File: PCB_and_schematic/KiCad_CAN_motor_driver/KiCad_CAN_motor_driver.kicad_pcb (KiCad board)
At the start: 2 copper layers, 90.4 x 45.2 mm, 67 parts, among them J1 SWDIO, J2 UART, J3 POWER IN 24V, J4 MOTOR OUT, J5 CAN, J6 PWM IN, Q1 BTN8982TA, Q2 BTN8982TA, U1 SN65HVD232, U2 LMR50410, U3 STM32F103C8Tx

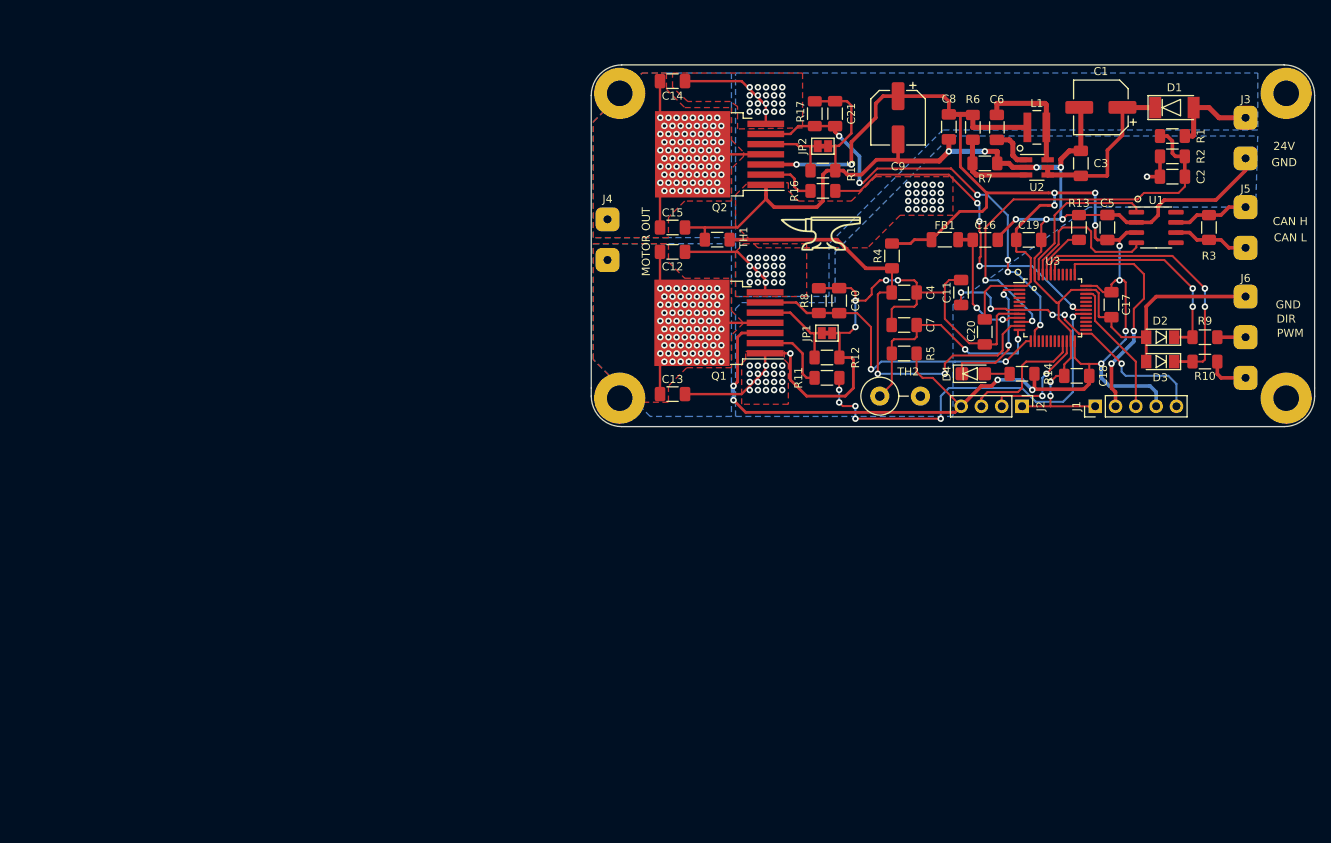
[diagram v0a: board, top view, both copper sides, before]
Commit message: Power traces optimization
+power traces optimized for lower resistance
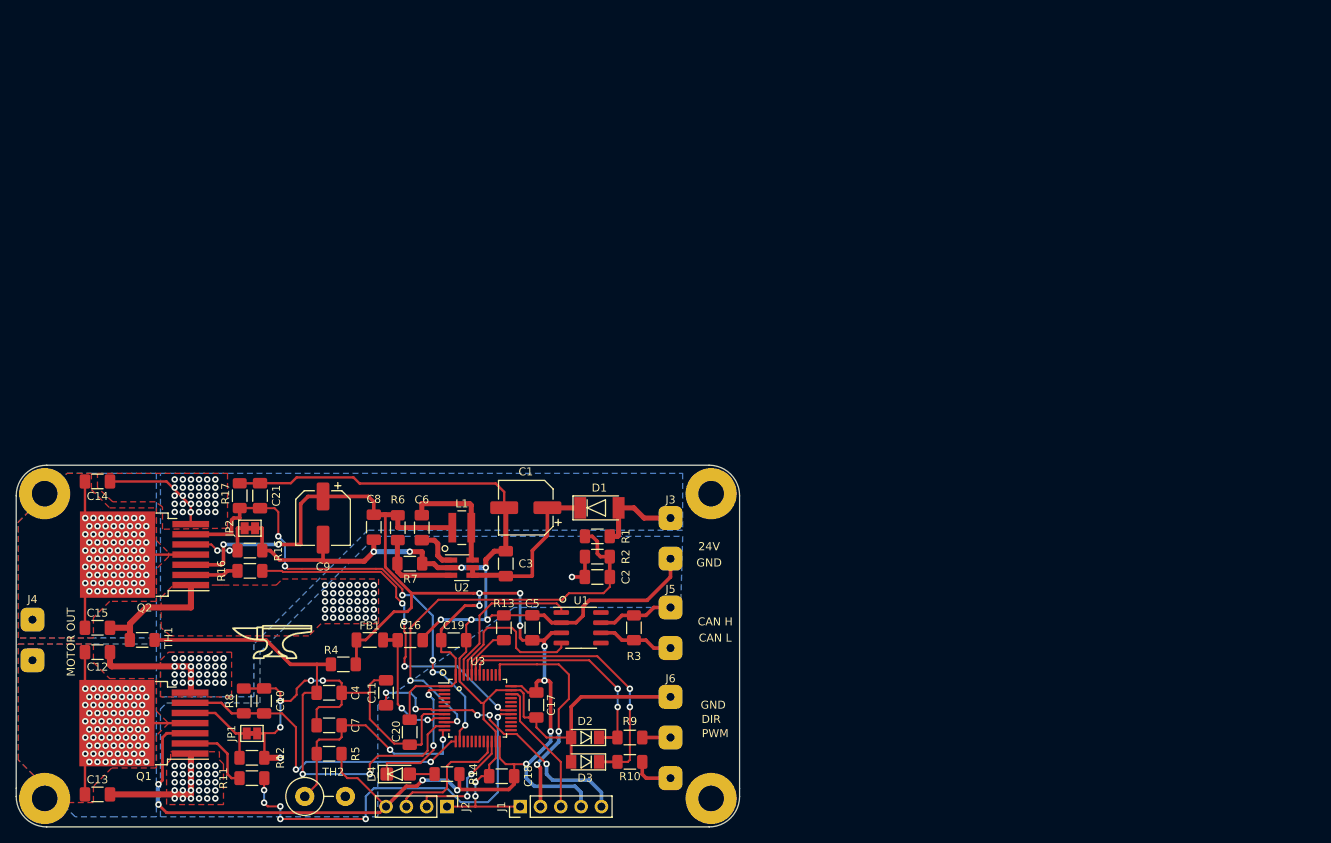
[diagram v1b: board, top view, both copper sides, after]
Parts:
- moved J3 87.6 mm to (187.7, 86.1)
- moved J5 87.6 mm to (187.7, 97.3)
- moved J6 87.6 mm to (187.7, 108.5)
- moved R10 87.6 mm to (182.6, 114.0)
- moved REF** 87.6 mm to (145.5, 81.5)
- moved TH2 87.6 mm to (142.0, 118.4)
- moved C1 87.6 mm to (169.6, 82.3)
- moved C10 87.6 mm to (136.9, 106.4)
- moved C11 87.6 mm to (152.1, 105.4)
- moved C12 87.6 mm to (116.1, 100.3)
- moved C13 87.6 mm to (116.1, 118.1)
- moved C14 87.6 mm to (116.1, 79.0)
- moved C15 87.6 mm to (116.1, 97.3)
- moved C16 87.6 mm to (155.2, 98.8)
- moved C17 87.6 mm to (170.9, 106.9)
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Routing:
- net GND: track 301.4 -> 296.8 mm, vias 55 -> 80
- net /I_SENSE_2: track 57.4 -> 61.2 mm
- net /NTC_INTERNAL: track 58.7 -> 60.8 mm
- net +24V: track 38.3 -> 40.4 mm, vias 40 -> 58
- net Net-(Q2-Pad2): track 7.03 -> 6.06 mm
- net +3V3: track 232.7 -> 233.5 mm
- net Net-(JP2-Pad1): track 9.65 -> 9.84 mm, vias 0 -> 2
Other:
- net class Default: clearance 0.2032 -> 0.127
- rule trace_clearance: 0.2032 -> 0.127
- board text added: "Rev 1.0"

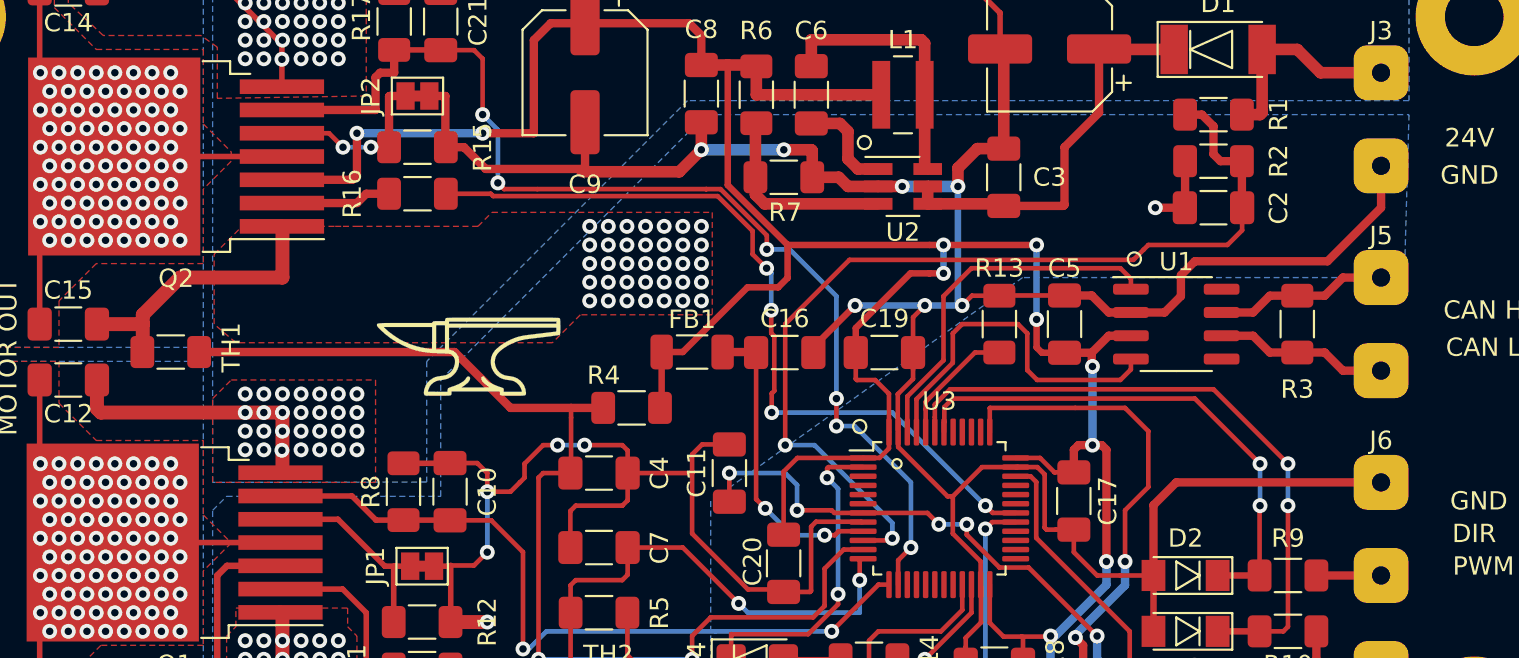
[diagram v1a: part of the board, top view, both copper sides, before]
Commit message: PDF schematic
+ schematic in PDF format for quick preview
+ changed resistors on PWM inputs from 1K to 6.8K to decrease Zener diodes current
+ little tweaks in PCB traces
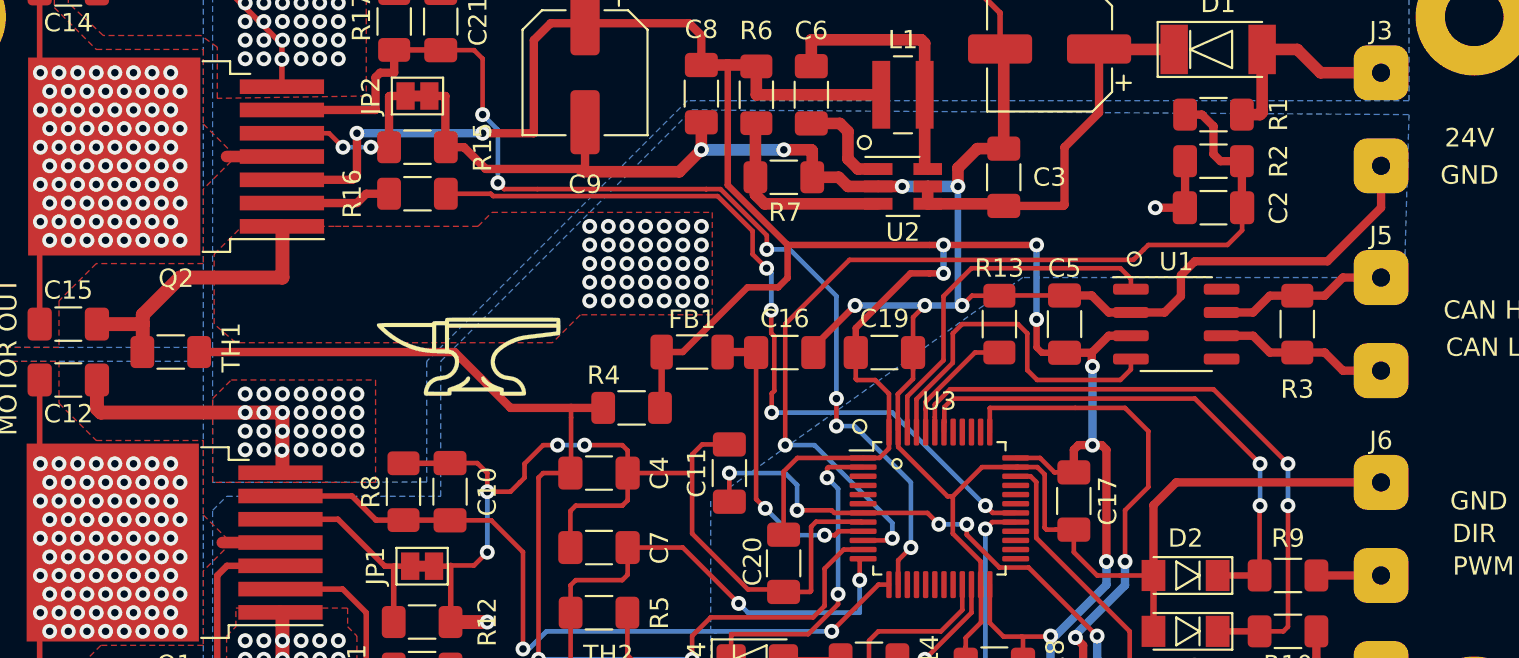
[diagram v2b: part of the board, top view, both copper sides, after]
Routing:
- net /MOT_B: track 30.8 -> 24.7 mm
- net /MOT_A: track 30.2 -> 24.3 mm
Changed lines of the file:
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@@
   (via (at 115.57 108.966) (size 0.8128) (drill 0.4064) (layers F.Cu B.Cu) (net 11))
   (via (at 119.634 110.998) (size 0.8128) (drill 0.4064) (layers F.Cu B.Cu) (net 11))
-  (segment (start 127.653 109.201) (end 118.503 109.201) (width 0.3048) (layer F.Cu) (net 11))
   (segment (start 114.5155 113.1885) (end 118.503 109.201) (width 0.3048) (layer F.Cu) (net 11))
   (segment (start 114.5155 118.11) (end 114.5155 113.1885) (width 0.3048) (layer F.Cu) (net 11))
   (segment (start 114.5155 105.2135) (end 118.503 109.201) (width 0.3048) (layer F.Cu) (net 11))
   (segment (start 114.5155 100.33) (end 114.5155 105.2135) (width 0.3048) (layer F.Cu) (net 11))
+  (segment (start 127.653 109.201) (end 124.479 109.201) (width 0.635) (layer F.Cu) (net 11))
   (via (at 130.81 80.772) (size 0.8128) (drill 0.4064) (layers F.Cu B.Cu) (net 12))
   (via (at 130.81 81.788) (size 0.8128) (drill 0.4064) (layers F.Cu B.Cu) (net 12))
@@
   (segment (start 114.5155 84.0705) (end 118.583 88.138) (width 0.3048) (layer F.Cu) (net 13))
   (segment (start 114.5155 78.994) (end 114.5155 84.0705) (width 0.3048) (layer F.Cu) (net 13))
-  (segment (start 127.733 88.138) (end 118.583 88.138) (width 0.3048) (layer F.Cu) (net 13))
   (segment (start 114.5155 92.2055) (end 118.583 88.138) (width 0.3048) (layer F.Cu) (net 13))
   (segment (start 114.5155 97.282) (end 114.5155 92.2055) (width 0.3048) (layer F.Cu) (net 13))
+  (segment (start 127.733 88.138) (end 124.714 88.138) (width 0.635) (layer F.Cu) (net 13))
   (segment (start 153.4435 98.9965) (end 153.606 98.834) (width 0.635) (layer F.Cu) (net 14))
   (via (at 154.106 107.334) (size 0.8128) (drill 0.4064) (layers F.Cu B.Cu) (net 14))
@@
       (pts
         (xy 188.976 94.742) (xy 168.148 94.742) (xy 151.13 106.934) (xy 151.13 120.904) (xy 123.952 120.904)
-        (xy 123.952 107.442) (xy 124.714 106.68) (xy 136.398 106.68) (xy 136.398 100.33) (xy 150.876 85.852)
+        (xy 123.952 107.442) (xy 124.714 106.68) (xy 136.398 106.68) (xy 136.398 99.314) (xy 150.114 85.598)
         (xy 189.23 85.852)
       )

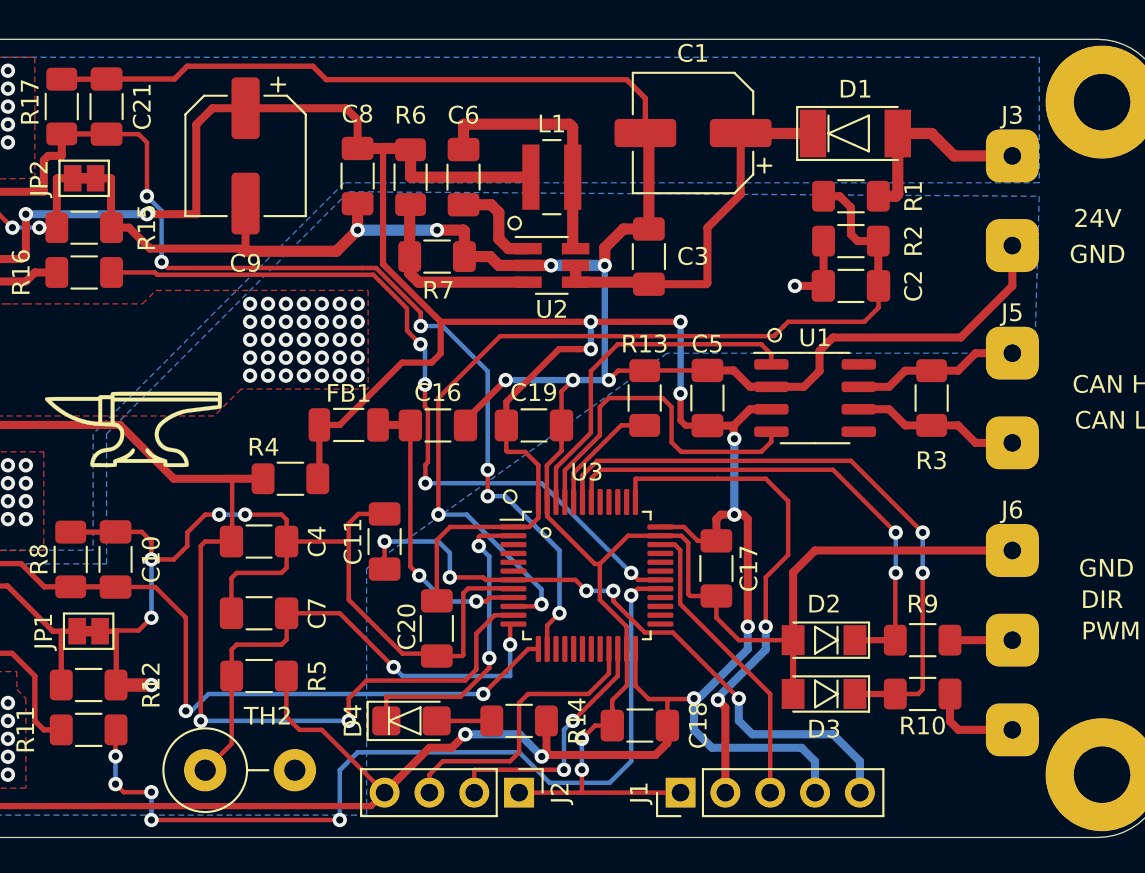
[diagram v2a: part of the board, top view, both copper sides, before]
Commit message: Added vias on power traces near input, added testpoints
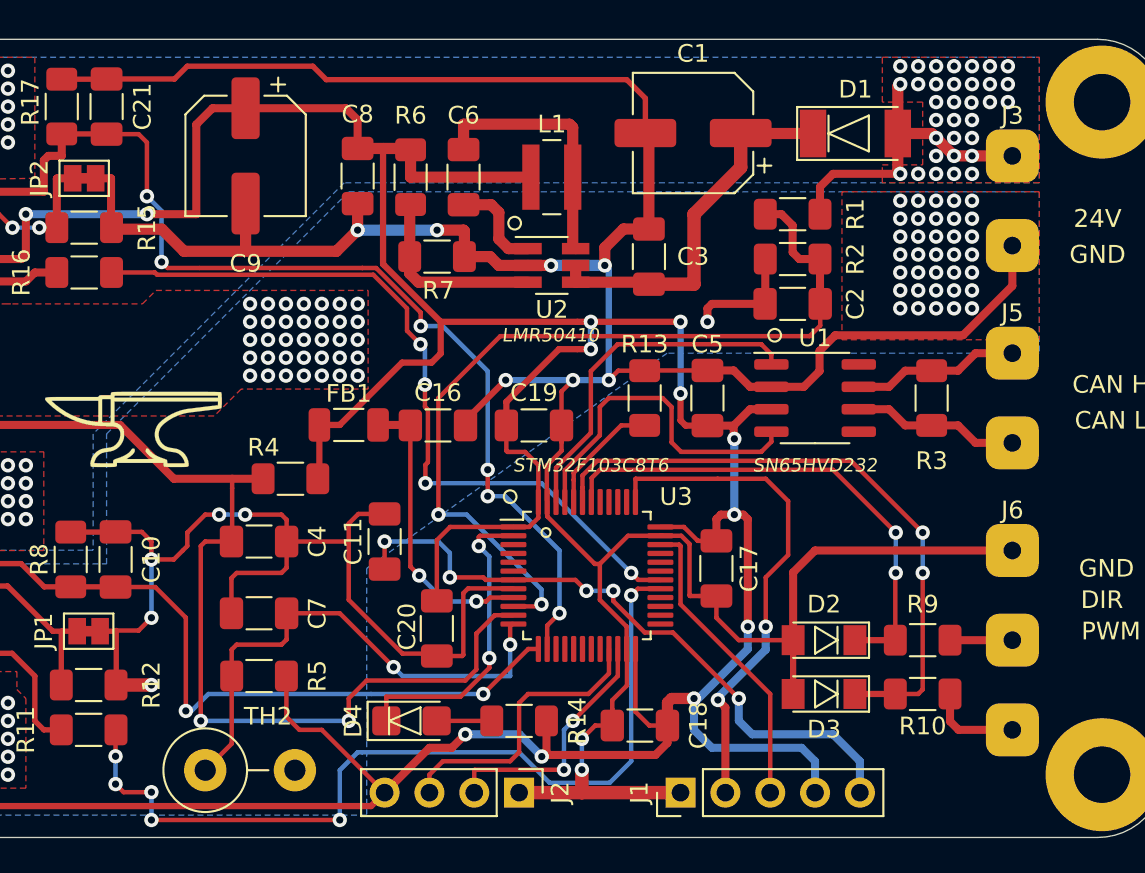
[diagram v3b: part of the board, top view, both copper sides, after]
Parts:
- moved R2 3.45 mm to (175.3, 89.4)
- moved C2 3.45 mm to (175.3, 91.9)
- moved R1 3.45 mm to (175.3, 86.9)
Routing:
- net +24V: track 40.4 -> 47.4 mm, vias 58 -> 91
- net /VIN: track 52.6 -> 48.8 mm
- net GND: track 296.8 -> 299.2 mm, vias 80 -> 115
- net +3V3: track 233.5 -> 234.9 mm
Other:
- board text added: "LMR50410"
- board text added: "SN65HVD232"
- board text added: "STM32F103C8T6"
